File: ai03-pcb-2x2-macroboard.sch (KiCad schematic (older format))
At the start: 14 parts

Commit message: Add MX-Matrix
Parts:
- added D? (x4): D_Small, symbol Device:D_Small
- added F?: Polyfuse, symbol Device:Polyfuse
- added MX? (x4): MX-NoLED, symbol MX_Alps_Hybrid:MX-NoLED
- added USB?: Molex-0548190589, symbol random-keyboard-parts:Molex-0548190589
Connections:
- net +5V: now also F?.1
- net D+: now also USB?.3 (D+)
- net D-: now also USB?.4 (D-)
- net GND: now also USB?.1 (GND)
- net ROW0: now reaches U?.27 (PD7)
- net ROW0: now also D?.1 (K), D?.1 (K)
- net COL1: now reaches U?.28 (PB4)
- net COL1: now also MX?.1 (COL), MX?.1 (COL)
- net COL0: now reaches U?.29 (PB5)
- net COL0: now also MX?.1 (COL), MX?.1 (COL)
- net ROW1: now reaches U?.30 (PB6)
- net ROW1: now also D?.1 (K), D?.1 (K)
- new net: D?.2 (A), MX?.2 (ROW) (x4)
- new net VCC: F?.2, USB?.5 (VBUS)
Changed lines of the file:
@@
 Text GLabel 1500 2800 0    50   Input ~ 0
 D-
+$Comp
+L random-keyboard-parts:Molex-0548190589 USB?
+U 1 1 5F2454B1
+P 5250 1850
+F 0 "USB?" V 5787 1817 60  0000 C CNN
+F 1 "Molex-0548190589" V 5681 1817 60  0000 C CNN
+F 2 "" H 5250 1850 60  0001 C CNN
+F 3 "" H 5250 1850 60  0001 C CNN
+	1    5250 1850
+	0    -1   -1   0
+$EndComp
+$Comp
+L power:VCC #PWR?
+U 1 1 5F24A7DF
+P 5900 1650
+F 0 "#PWR?" H 5900 1500 50  0001 C CNN
+F 1 "VCC" H 5917 1823 50  0000 C CNN
+F 2 "" H 5900 1650 50  0001 C CNN
+F 3 "" H 5900 1650 50  0001 C CNN
+	1    5900 1650
+	1    0    0    -1
+$EndComp
+$Comp
+L Device:Polyfuse F?
+U 1 1 5F24B6BA
+P 6350 1650
+F 0 "F?" V 6125 1650 50  0000 C CNN
+F 1 "Polyfuse" V 6216 1650 50  0000 C CNN
+F 2 "" H 6400 1450 50  0001 L CNN
+F 3 "~" H 6350 1650 50  0001 C CNN
+	1    6350 1650
+	0    1    1    0
+$EndComp
+$Comp
+L power:+5V #PWR?
+U 1 1 5F24C036
+P 6800 1650
+F 0 "#PWR?" H 6800 1500 50  0001 C CNN
+F 1 "+5V" H 6815 1823 50  0000 C CNN
+F 2 "" H 6800 1650 50  0001 C CNN
+F 3 "" H 6800 1650 50  0001 C CNN
+	1    6800 1650
+	1    0    0    -1
+$EndComp
+Wire Wire Line
+	6800 1650 6500 1650
+Wire Wire Line
+	6200 1650 5900 1650
+Connection ~ 5900 1650
+Wire Wire Line
+	5900 1650 5550 1650
+Text GLabel 5550 1750 2    50   Input ~ 0
+D-
+Text GLabel 5550 1850 2    50   Input ~ 0
+D+
+$Comp
+L power:GND #PWR?
+U 1 1 5F250A84
+P 5550 2050
+F 0 "#PWR?" H 5550 1800 50  0001 C CNN
+F 1 "GND" H 5555 1877 50  0000 C CNN
+F 2 "" H 5550 2050 50  0001 C CNN
+F 3 "" H 5550 2050 50  0001 C CNN
+	1    5550 2050
+	1    0    0    -1
+$EndComp
+$Comp
+L MX_Alps_Hybrid:MX-NoLED MX?
+U 1 1 5F251C5F
+P 6750 3350
+F 0 "MX?" H 6783 3573 60  0000 C CNN
+F 1 "MX-NoLED" H 6783 3499 20  0000 C CNN
+F 2 "" H 6125 3325 60  0001 C CNN
+F 3 "" H 6125 3325 60  0001 C CNN
+	1    6750 3350
+	1    0    0    -1
+$EndComp
+$Comp
+L Device:D_Small D?
+U 1 1 5F252F27
+P 6500 3600
+F 0 "D?" V 6546 3532 50  0000 R CNN
+F 1 "D_Small" V 6455 3532 50  0000 R CNN
+F 2 "" V 6500 3600 50  0001 C CNN
+F 3 "~" V 6500 3600 50  0001 C CNN
+	1    6500 3600
+	0    -1   -1   0
+$EndComp
+Wire Wire Line
+	6500 3500 6700 3500
+$Comp
+L MX_Alps_Hybrid:MX-NoLED MX?
+U 1 1 5F256A5E
+P 7350 3350
+F 0 "MX?" H 7383 3573 60  0000 C CNN
+F 1 "MX-NoLED" H 7383 3499 20  0000 C CNN
+F 2 "" H 6725 3325 60  0001 C CNN
+F 3 "" H 6725 3325 60  0001 C CNN
+	1    7350 3350
+	1    0    0    -1
+$EndComp
+$Comp
+L Device:D_Small D?
+U 1 1 5F256A64
+P 7100 3600
+F 0 "D?" V 7146 3532 50  0000 R CNN
+F 1 "D_Small" V 7055 3532 50  0000 R CNN
+F 2 "" V 7100 3600 50  0001 C CNN
+F 3 "~" V 7100 3600 50  0001 C CNN
+	1    7100 3600
+	0    -1   -1   0
+$EndComp
+Wire Wire Line
+	7100 3500 7300 3500
+$Comp
+L MX_Alps_Hybrid:MX-NoLED MX?
+U 1 1 5F259A2B
+P 6750 4050
+F 0 "MX?" H 6783 4273 60  0000 C CNN
+F 1 "MX-NoLED" H 6783 4199 20  0000 C CNN
+F 2 "" H 6125 4025 60  0001 C CNN
+F 3 "" H 6125 4025 60  0001 C CNN
+	1    6750 4050
+	1    0    0    -1
+$EndComp
+$Comp
+L Device:D_Small D?
+U 1 1 5F259A31
+P 6500 4300
+F 0 "D?" V 6546 4232 50  0000 R CNN
+F 1 "D_Small" V 6455 4232 50  0000 R CNN
+F 2 "" V 6500 4300 50  0001 C CNN
+F 3 "~" V 6500 4300 50  0001 C CNN
+	1    6500 4300
+	0    -1   -1   0
+$EndComp
+Wire Wire Line
+	6500 4200 6700 4200
+$Comp
+L MX_Alps_Hybrid:MX-NoLED MX?
+U 1 1 5F25AA31
+P 7350 4050
+F 0 "MX?" H 7383 4273 60  0000 C CNN
+F 1 "MX-NoLED" H 7383 4199 20  0000 C CNN
+F 2 "" H 6725 4025 60  0001 C CNN
+F 3 "" H 6725 4025 60  0001 C CNN
+	1    7350 4050
+	1    0    0    -1
+$EndComp
+$Comp
+L Device:D_Small D?
+U 1 1 5F25AA37
+P 7100 4300
+F 0 "D?" V 7146 4232 50  0000 R CNN
+F 1 "D_Small" V 7055 4232 50  0000 R CNN
+F 2 "" V 7100 4300 50  0001 C CNN
+F 3 "~" V 7100 4300 50  0001 C CNN
+	1    7100 4300
+	0    -1   -1   0
+$EndComp
+Wire Wire Line
+	7100 4200 7300 4200
+Wire Wire Line
+	7100 3700 6500 3700
+Connection ~ 6500 3700
+Wire Wire Line
+	6500 3700 6000 3700
+Wire Wire Line
+	7100 4400 6500 4400
+Wire Wire Line
+	6900 4000 6900 3300
+Connection ~ 6900 3300
+Wire Wire Line
+	7500 4000 7500 3300
+Connection ~ 7500 3300
+Wire Wire Line
+	7500 3300 7500 2700
+Wire Wire Line
+	6900 2700 6900 3300
+Text GLabel 6000 3700 0    50   Input ~ 0
+ROW0
+Text GLabel 6000 4400 0    50   Input ~ 0
+ROW1
+Wire Wire Line
+	6000 4400 6500 4400
+Connection ~ 6500 4400
+Text GLabel 6900 2700 1    50   Input ~ 0
+COL0
+Text GLabel 7500 2700 1    50   Input ~ 0
+COL1
+Text GLabel 4100 2100 2    50   Input ~ 0
+COL1
+Text GLabel 4100 2200 2    50   Input ~ 0
+COL0
+Text GLabel 4100 2300 2    50   Input ~ 0
+ROW1
+Text GLabel 4100 3600 2    50   Input ~ 0
+ROW0
 $EndSCHEMATC

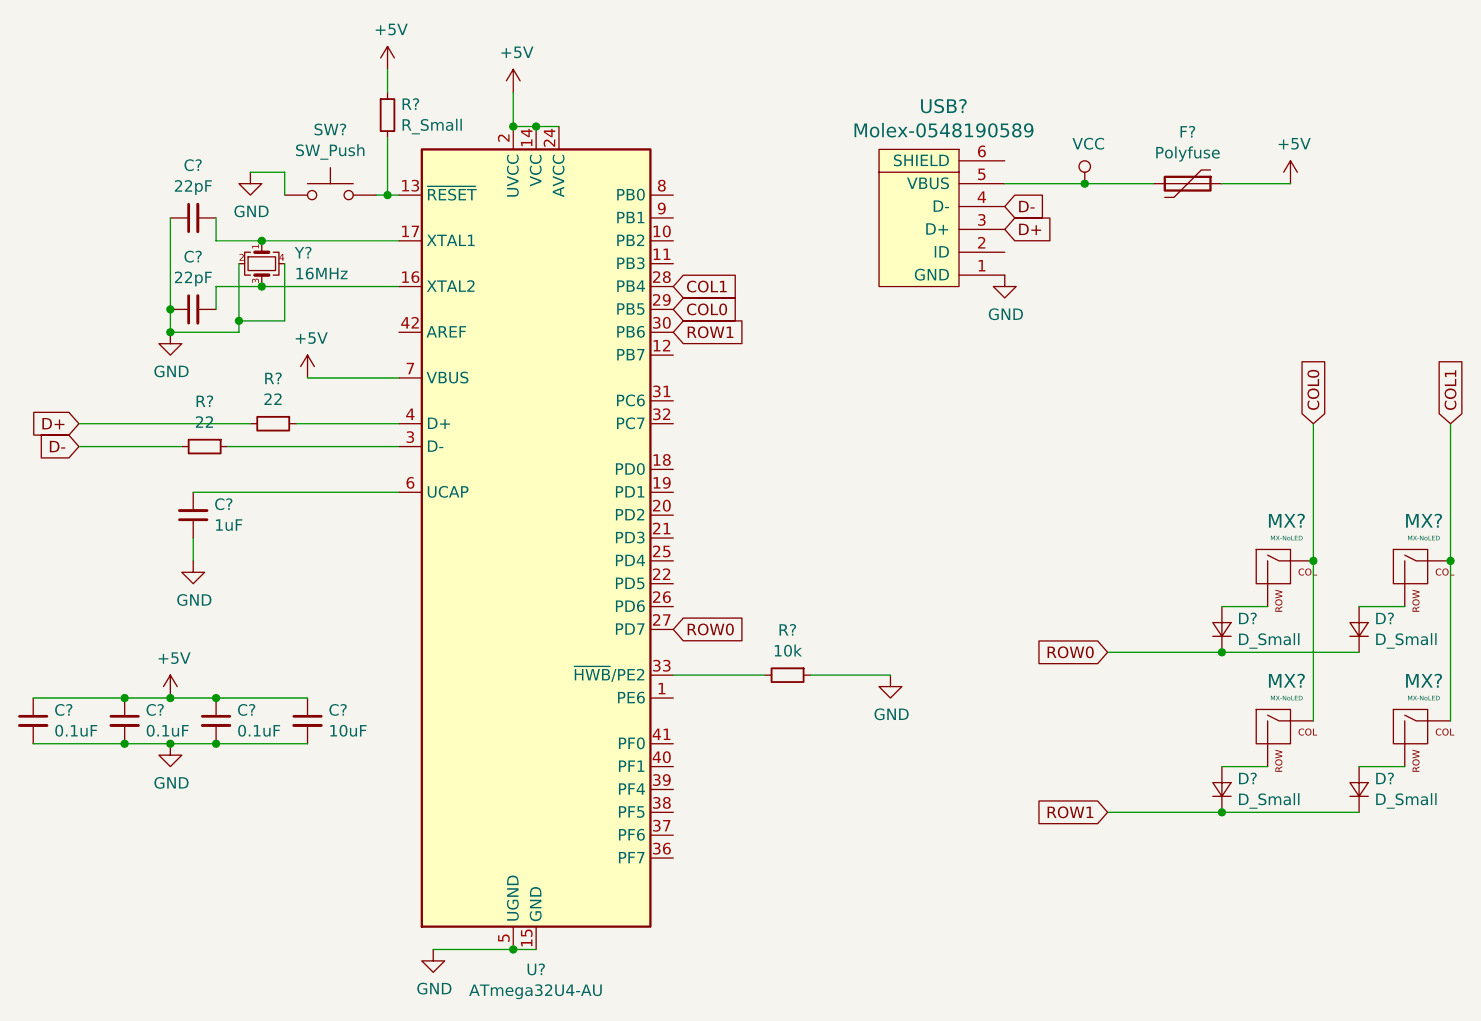
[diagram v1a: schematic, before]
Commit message: Add footprints
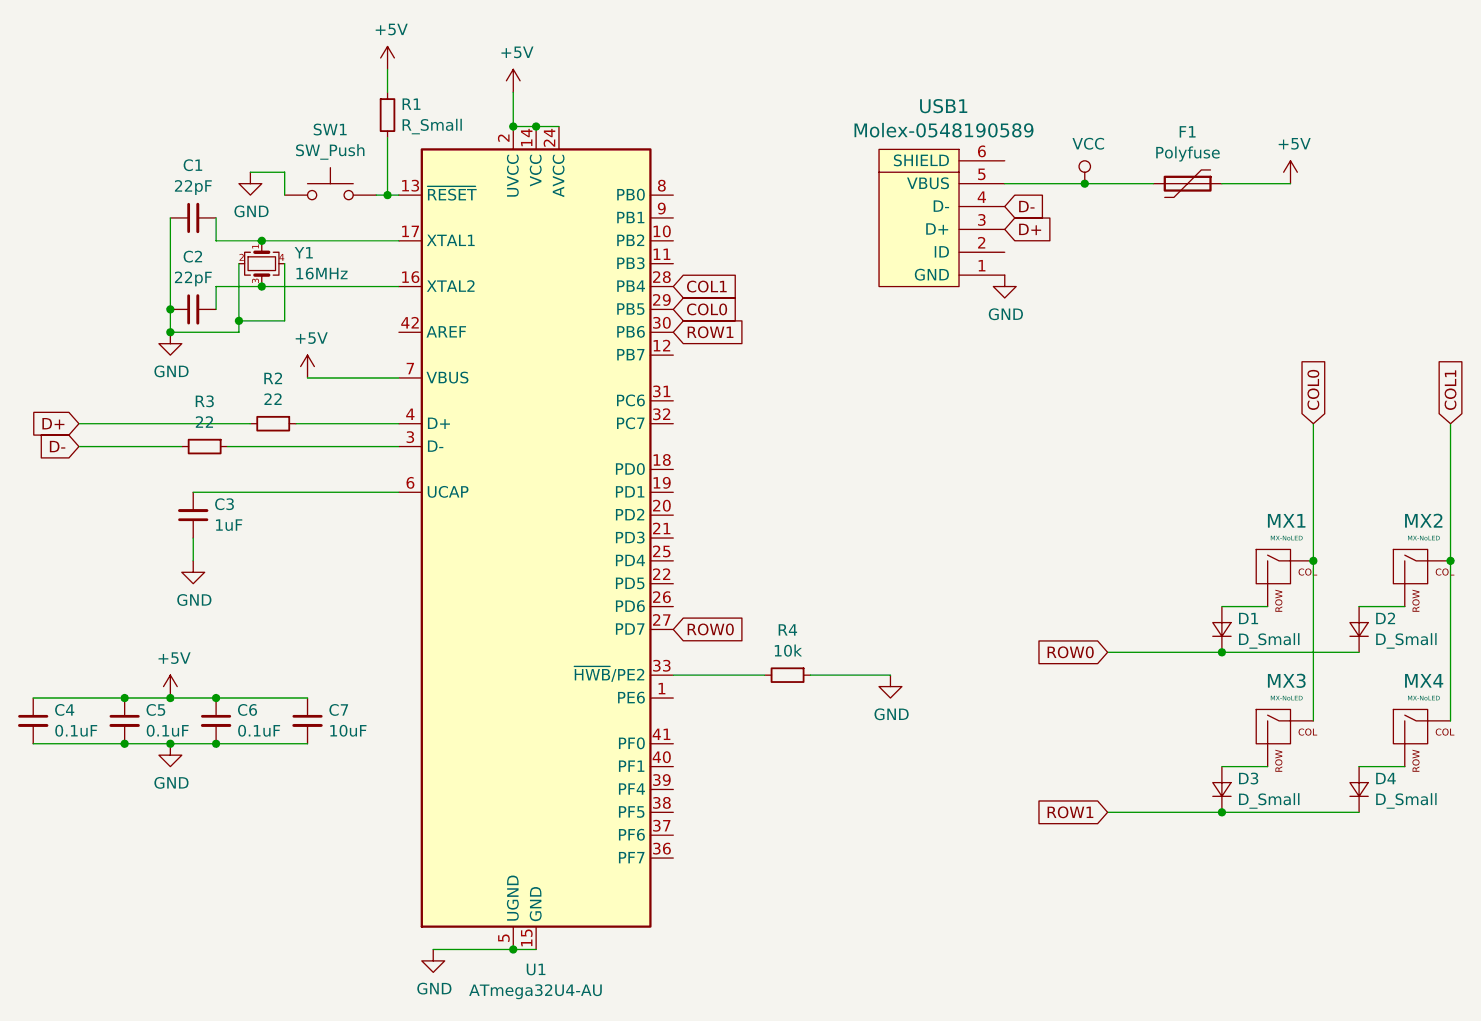
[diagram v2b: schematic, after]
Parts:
- C1, C2, C3, C4, C5, C6, C7: renamed from C?; footprint (none) -> Capacitor_SMD:C_0805_2012Metric
- D1, D2, D3, D4: renamed from D?; footprint (none) -> Diode_SMD:D_SOD-123
- F1: renamed from F?; footprint (none) -> Fuse:Fuse_1206_3216Metric
- MX1, MX2, MX3, MX4: renamed from MX?; footprint (none) -> MX_Alps_Hybrid:MX-1U
- R1, R2, R3, R4: renamed from R?; footprint (none) -> Resistor_SMD:R_0805_2012Metric
- SW1: renamed from SW?; footprint (none) -> random-keyboard-parts:SKQG-1155865
- USB1: renamed from USB?; footprint (none) -> random-keyboard-parts:Molex-0548190589
- Y1: renamed from Y?; footprint (none) -> Crystal:Crystal_SMD_3225-4Pin_3.2x2.5mm
- gave numbers to parts that had none: 1

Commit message: Update Schematic
I forgot some labels etc. so here they are.
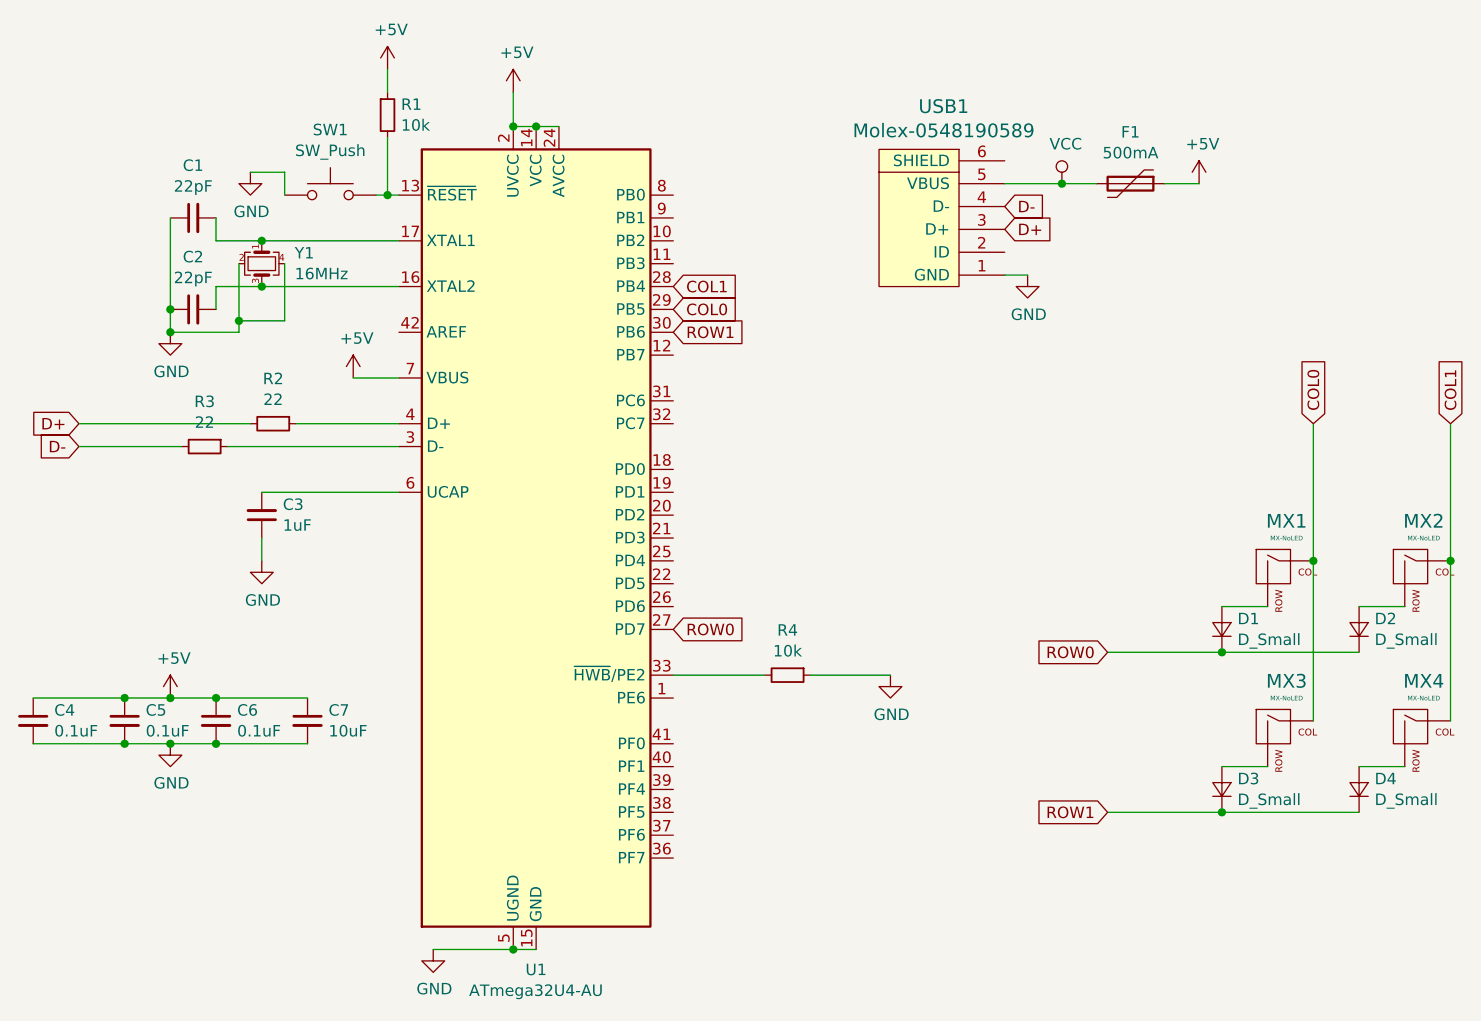
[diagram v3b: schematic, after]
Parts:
- F1: value Polyfuse -> 500mA
- R1: value R_Small -> 10k
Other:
- moved on the sheet: C3, F1
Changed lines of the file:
@@
 EESchema Schematic File Version 4
+LIBS:ai03-pcb-2x2-macroboard-cache
 EELAYER 30 0
 EELAYER END
@@
 L Device:C_Small C3
 U 1 1 5F21FCAD
-P 2000 3100
-F 0 "C3" H 1908 3054 50  0000 R CNN
-F 1 "1uF" H 1908 3145 50  0000 R CNN
-F 2 "Capacitor_SMD:C_0805_2012Metric" H 2000 3100 50  0001 C CNN
-F 3 "~" H 2000 3100 50  0001 C CNN
-	1    2000 3100
+P 2300 3100
+F 0 "C3" H 2208 3054 50  0000 R CNN
+F 1 "1uF" H 2208 3145 50  0000 R CNN
+F 2 "Capacitor_SMD:C_0805_2012Metric" H 2300 3100 50  0001 C CNN
+F 3 "~" H 2300 3100 50  0001 C CNN
+	1    2300 3100
 	-1   0    0    1
 $EndComp
-Wire Wire Line
-	2000 3000 2900 3000
 $Comp
 L power:GND #PWR0104
 U 1 1 5F221A2C
-P 2000 3300
-F 0 "#PWR0104" H 2000 3050 50  0001 C CNN
-F 1 "GND" H 2005 3127 50  0000 C CNN
-F 2 "" H 2000 3300 50  0001 C CNN
-F 3 "" H 2000 3300 50  0001 C CNN
-	1    2000 3300
-	1    0    0    -1
-$EndComp
-Wire Wire Line
-	2000 3200 2000 3300
+P 2300 3300
+F 0 "#PWR0104" H 2300 3050 50  0001 C CNN
+F 1 "GND" H 2305 3127 50  0000 C CNN
+F 2 "" H 2300 3300 50  0001 C CNN
+F 3 "" H 2300 3300 50  0001 C CNN
+	1    2300 3300
+	1    0    0    -1
+$EndComp
+Wire Wire Line
+	2300 3200 2300 3300
 $Comp
 L Device:C_Small C4
@@
 L power:+5V #PWR0107
 U 1 1 5F22B582
-P 2500 2500
-F 0 "#PWR0107" H 2500 2350 50  0001 C CNN
-F 1 "+5V" H 2515 2673 50  0000 C CNN
-F 2 "" H 2500 2500 50  0001 C CNN
-F 3 "" H 2500 2500 50  0001 C CNN
-	1    2500 2500
-	1    0    0    -1
-$EndComp
-Wire Wire Line
-	2500 2500 2900 2500
+P 2700 2500
+F 0 "#PWR0107" H 2700 2350 50  0001 C CNN
+F 1 "+5V" H 2715 2673 50  0000 C CNN
+F 2 "" H 2700 2500 50  0001 C CNN
+F 3 "" H 2700 2500 50  0001 C CNN
+	1    2700 2500
+	1    0    0    -1
+$EndComp
+Wire Wire Line
+	2700 2500 2900 2500
 $Comp
 L Device:Crystal_GND24_Small Y1
@@
 P 2850 1350
 F 0 "R1" H 2909 1396 50  0000 L CNN
-F 1 "R_Small" H 2909 1305 50  0000 L CNN
+F 1 "10k" H 2909 1305 50  0000 L CNN
 F 2 "Resistor_SMD:R_0805_2012Metric" H 2850 1350 50  0001 C CNN
 F 3 "~" H 2850 1350 50  0001 C CNN
@@
 L power:VCC #PWR0111
 U 1 1 5F24A7DF
-P 5900 1650
-F 0 "#PWR0111" H 5900 1500 50  0001 C CNN
-F 1 "VCC" H 5917 1823 50  0000 C CNN
-F 2 "" H 5900 1650 50  0001 C CNN
-F 3 "" H 5900 1650 50  0001 C CNN
-	1    5900 1650
+P 5800 1650
+F 0 "#PWR0111" H 5800 1500 50  0001 C CNN
+F 1 "VCC" H 5817 1823 50  0000 C CNN
+F 2 "" H 5800 1650 50  0001 C CNN
+F 3 "" H 5800 1650 50  0001 C CNN
+	1    5800 1650
 	1    0    0    -1
 $EndComp
@@
 L Device:Polyfuse F1
 U 1 1 5F24B6BA
-P 6350 1650
-F 0 "F1" V 6125 1650 50  0000 C CNN
-F 1 "Polyfuse" V 6216 1650 50  0000 C CNN
-F 2 "Fuse:Fuse_1206_3216Metric" H 6400 1450 50  0001 L CNN
-F 3 "~" H 6350 1650 50  0001 C CNN
-	1    6350 1650
+P 6100 1650
+F 0 "F1" V 5875 1650 50  0000 C CNN
+F 1 "500mA" V 5966 1650 50  0000 C CNN
+F 2 "Fuse:Fuse_1206_3216Metric" H 6150 1450 50  0001 L CNN
+F 3 "~" H 6100 1650 50  0001 C CNN
+	1    6100 1650
 	0    1    1    0
 $EndComp
@@
 L power:+5V #PWR0112
 U 1 1 5F24C036
-P 6800 1650
-F 0 "#PWR0112" H 6800 1500 50  0001 C CNN
-F 1 "+5V" H 6815 1823 50  0000 C CNN
-F 2 "" H 6800 1650 50  0001 C CNN
-F 3 "" H 6800 1650 50  0001 C CNN
-	1    6800 1650
-	1    0    0    -1
-$EndComp
-Wire Wire Line
-	6800 1650 6500 1650
-Wire Wire Line
-	6200 1650 5900 1650
-Connection ~ 5900 1650
-Wire Wire Line
-	5900 1650 5550 1650
+P 6400 1650
+F 0 "#PWR0112" H 6400 1500 50  0001 C CNN
+F 1 "+5V" H 6415 1823 50  0000 C CNN
+F 2 "" H 6400 1650 50  0001 C CNN
+F 3 "" H 6400 1650 50  0001 C CNN
+	1    6400 1650
+	1    0    0    -1
+$EndComp
+Wire Wire Line
+	6400 1650 6250 1650
+Wire Wire Line
+	5950 1650 5800 1650
+Connection ~ 5800 1650
+Wire Wire Line
+	5800 1650 5550 1650
 Text GLabel 5550 1750 2    50   Input ~ 0
 D-
@@
 L power:GND #PWR0113
 U 1 1 5F250A84
-P 5550 2050
-F 0 "#PWR0113" H 5550 1800 50  0001 C CNN
-F 1 "GND" H 5555 1877 50  0000 C CNN
-F 2 "" H 5550 2050 50  0001 C CNN
-F 3 "" H 5550 2050 50  0001 C CNN
-	1    5550 2050
+P 5650 2050
+F 0 "#PWR0113" H 5650 1800 50  0001 C CNN
+F 1 "GND" H 5655 1877 50  0000 C CNN
+F 2 "" H 5650 2050 50  0001 C CNN
+F 3 "" H 5650 2050 50  0001 C CNN
+	1    5650 2050
 	1    0    0    -1
 $EndComp
@@
 Text GLabel 4100 3600 2    50   Input ~ 0
 ROW0
+Wire Wire Line
+	2300 3000 2900 3000
+Wire Wire Line
+	5550 2050 5650 2050
 $EndSCHEMATC
